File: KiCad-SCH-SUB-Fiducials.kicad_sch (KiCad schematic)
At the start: 4 parts

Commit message: fix: fiducials to nobom
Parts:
- FID1, FID2, FID3, FID4: now left out of the parts list
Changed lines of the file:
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@@
   )
   (symbol (lib_id "Mechanical:Fiducial") (at 96.52 60.96 0) (unit 1)
-    (in_bom yes) (on_board yes) (dnp no) (fields_autoplaced)
+    (in_bom no) (on_board yes) (dnp no) (fields_autoplaced)
     (property "Reference" "FID1" (at 99.06 60.325 0)
       (effects (font (size 1.27 1.27)) (justify left))
@@
     )
     (instances
-      (project "KiCad-SCH-SUB"
+      (project "KiCad-SCH-SUB-Fiducials"
         (path "/d38811ea-76f9-423e-a00e-9090662f3ef7"
           (reference "FID1") (unit 1)
@@
   )
   (symbol (lib_id "Mechanical:Fiducial") (at 96.52 76.2 0) (unit 1)
-    (in_bom yes) (on_board yes) (dnp no) (fields_autoplaced)
+    (in_bom no) (on_board yes) (dnp no) (fields_autoplaced)
     (property "Reference" "FID4" (at 99.06 75.565 0)
       (effects (font (size 1.27 1.27)) (justify left))
@@
     )
     (instances
-      (project "KiCad-SCH-SUB"
+      (project "KiCad-SCH-SUB-Fiducials"
         (path "/d38811ea-76f9-423e-a00e-9090662f3ef7"
           (reference "FID4") (unit 1)
@@
   )
   (symbol (lib_id "Mechanical:Fiducial") (at 96.52 71.12 0) (unit 1)
-    (in_bom yes) (on_board yes) (dnp no) (fields_autoplaced)
+    (in_bom no) (on_board yes) (dnp no) (fields_autoplaced)
     (property "Reference" "FID3" (at 99.06 70.485 0)
       (effects (font (size 1.27 1.27)) (justify left))
@@
     )
     (instances
-      (project "KiCad-SCH-SUB"
+      (project "KiCad-SCH-SUB-Fiducials"
         (path "/d38811ea-76f9-423e-a00e-9090662f3ef7"
           (reference "FID3") (unit 1)
@@
   )
   (symbol (lib_id "Mechanical:Fiducial") (at 96.52 66.04 0) (unit 1)
-    (in_bom yes) (on_board yes) (dnp no) (fields_autoplaced)
+    (in_bom no) (on_board yes) (dnp no) (fields_autoplaced)
     (property "Reference" "FID2" (at 99.06 65.405 0)
       (effects (font (size 1.27 1.27)) (justify left))
@@
     )
     (instances
-      (project "KiCad-SCH-SUB"
+      (project "KiCad-SCH-SUB-Fiducials"
         (path "/d38811ea-76f9-423e-a00e-9090662f3ef7"
           (reference "FID2") (unit 1)

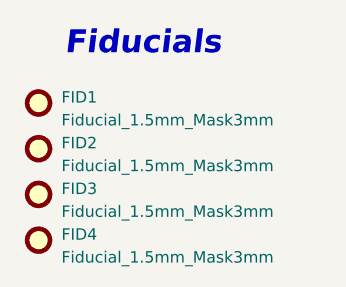
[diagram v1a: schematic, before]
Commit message: fix: change footprint to bigger
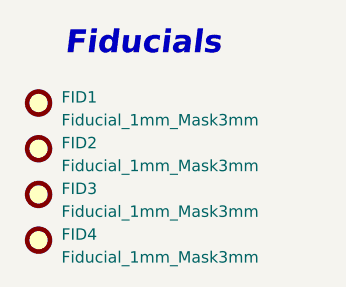
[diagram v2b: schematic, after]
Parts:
- FID1, FID2, FID3, FID4: value Fiducial_1.5mm_Mask3mm -> Fiducial_1mm_Mask3mm; footprint Fiducial:Fiducial_1.5mm_Mask3mm -> Fiducial:Fiducial_1mm_Mask3mm
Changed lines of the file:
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@@
       (effects (font (size 1.27 1.27)) (justify left))
     )
-    (property "Value" "Fiducial_1.5mm_Mask3mm" (at 99.06 62.865 0)
+    (property "Value" "Fiducial_1mm_Mask3mm" (at 99.06 62.865 0)
       (effects (font (size 1.27 1.27)) (justify left))
     )
-    (property "Footprint" "Fiducial:Fiducial_1.5mm_Mask3mm" (at 96.52 60.96 0)
+    (property "Footprint" "Fiducial:Fiducial_1mm_Mask3mm" (at 96.52 60.96 0)
       (effects (font (size 1.27 1.27)) hide)
     )
@@
       (effects (font (size 1.27 1.27)) (justify left))
     )
-    (property "Value" "Fiducial_1.5mm_Mask3mm" (at 99.06 78.105 0)
+    (property "Value" "Fiducial_1mm_Mask3mm" (at 99.06 78.105 0)
       (effects (font (size 1.27 1.27)) (justify left))
     )
-    (property "Footprint" "Fiducial:Fiducial_1.5mm_Mask3mm" (at 96.52 76.2 0)
+    (property "Footprint" "Fiducial:Fiducial_1mm_Mask3mm" (at 96.52 76.2 0)
       (effects (font (size 1.27 1.27)) hide)
     )
@@
       (effects (font (size 1.27 1.27)) (justify left))
     )
-    (property "Value" "Fiducial_1.5mm_Mask3mm" (at 99.06 73.025 0)
+    (property "Value" "Fiducial_1mm_Mask3mm" (at 99.06 73.025 0)
       (effects (font (size 1.27 1.27)) (justify left))
     )
-    (property "Footprint" "Fiducial:Fiducial_1.5mm_Mask3mm" (at 96.52 71.12 0)
+    (property "Footprint" "Fiducial:Fiducial_1mm_Mask3mm" (at 96.52 71.12 0)
       (effects (font (size 1.27 1.27)) hide)
     )
@@
       (effects (font (size 1.27 1.27)) (justify left))
     )
-    (property "Value" "Fiducial_1.5mm_Mask3mm" (at 99.06 67.945 0)
+    (property "Value" "Fiducial_1mm_Mask3mm" (at 99.06 67.945 0)
       (effects (font (size 1.27 1.27)) (justify left))
     )
-    (property "Footprint" "Fiducial:Fiducial_1.5mm_Mask3mm" (at 96.52 66.04 0)
+    (property "Footprint" "Fiducial:Fiducial_1mm_Mask3mm" (at 96.52 66.04 0)
       (effects (font (size 1.27 1.27)) hide)
     )
